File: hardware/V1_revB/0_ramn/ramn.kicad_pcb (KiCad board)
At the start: 2 copper layers, 85.6 x 54 mm, 108 parts, among them J2 Screw_Terminal_01x03, J3 , J4 , J5 , J6 , P1 USB_C_Plug_USB2.0, U1 ATA6561-GAQW-N, U10 ATA6561-GAQW-N, U11 STM32L552/STM32L562, U12 NCV8163, U2 STM32L552/STM32L562, U3 NCV8163, U4 ATA6561-GAQW-N, U5 STM32L552/STM32L562, U6 NCV8163, U7 ATA6561-GAQW-N, U8 STM32L552/STM32L562, U9 NCV8163, Y1 NX3225GD-8MHZ-STD-CRA-3, Y2 NX3225GD-8MHZ-STD-CRA-3, Y3 NX3225GD-8MHZ-STD-CRA-3, Y4 NX3225GD-8MHZ-STD-CRA-3

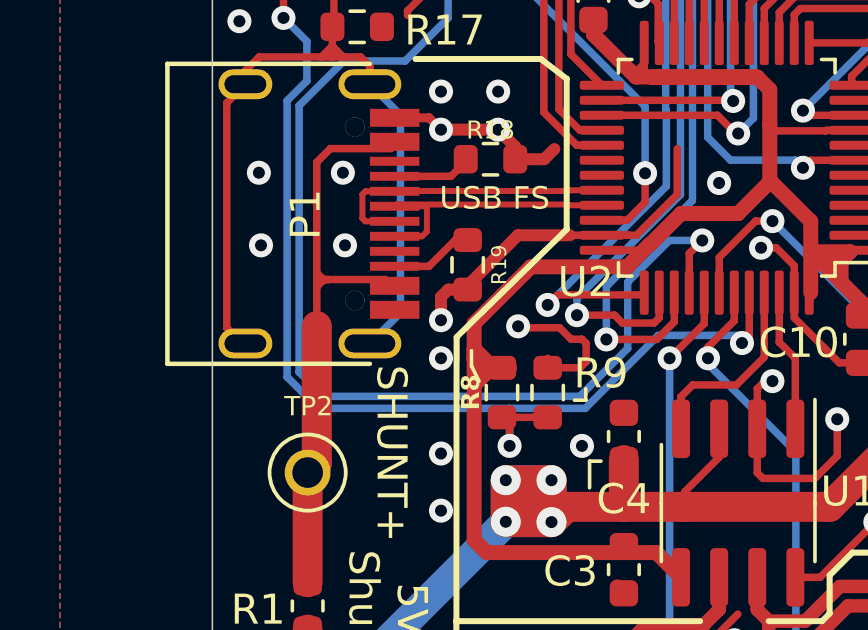
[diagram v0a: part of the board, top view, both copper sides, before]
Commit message: Feat(Hw): Modify_and_fix_footprints_and_symbols
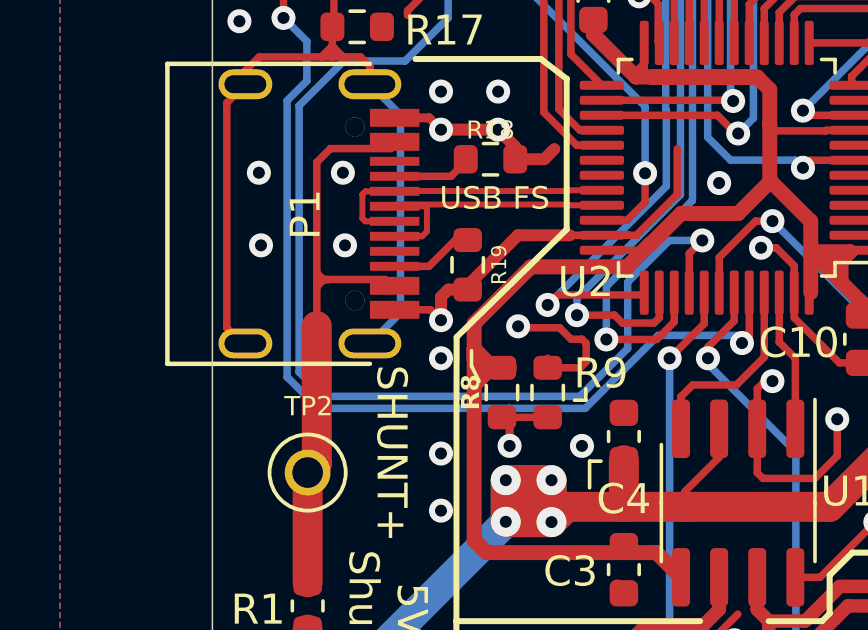
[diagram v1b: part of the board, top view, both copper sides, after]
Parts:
- BOOT0, J3, J4, J5, J6, RX1, TP1, TP10, TP2, TP3, TP4, TP5, TP6, TP7, TP8, TP9, TX1: value (none) -> ~
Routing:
- net GND: track 357.4 -> 359.1 mm
